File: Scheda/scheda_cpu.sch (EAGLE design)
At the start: 38 parts, among them IC2 LM3801N, IC3 LD1117V33

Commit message: modificato pcb
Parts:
- added H1, H2, H3: MOUNT-HOLE3.0, ITIS:MOUNT-HOLE3.0
- added LED: AK500, roombarmato_eagle_lib:AK500
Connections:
- net CHK_VBAT: now also IC1.A5; no longer IC1.A4
- net GND: now also LED.P$1
- net LED: now also IC1.A4, LED.P$2; no longer IC1.A5
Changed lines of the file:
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@@
 <part name="GND16" library="roombarmato_eagle_lib" deviceset="GND" device=""/>
 <part name="P+7" library="roombarmato_eagle_lib" deviceset="+12V" device=""/>
+<part name="LED" library="roombarmato_eagle_lib" deviceset="AK500" device="" package3d_urn="urn:adsk.eagle:package:17855270/2"/>
+<part name="GND17" library="roombarmato_eagle_lib" deviceset="GND" device=""/>
+<part name="H1" library="ITIS" deviceset="MOUNT-HOLE" device="3.0"/>
+<part name="H2" library="ITIS" deviceset="MOUNT-HOLE" device="3.0"/>
+<part name="H3" library="ITIS" deviceset="MOUNT-HOLE" device="3.0"/>
 </parts>
 <sheets>
@@
 <attribute name="VALUE" x="35.56" y="40.64" size="1.778" layer="96" rot="R90"/>
 </instance>
+<instance part="LED" gate="G$1" x="119.38" y="-34.29" smashed="yes">
+<attribute name="NAME" x="116.84" y="-27.94" size="1.27" layer="95"/>
+</instance>
+<instance part="GND17" gate="1" x="111.76" y="-40.64" smashed="yes">
+<attribute name="VALUE" x="109.22" y="-43.18" size="1.778" layer="96"/>
+</instance>
+<instance part="H1" gate="G$1" x="74.93" y="-30.48" smashed="yes">
+<attribute name="NAME" x="76.962" y="-29.8958" size="1.778" layer="95"/>
+<attribute name="VALUE" x="76.962" y="-32.9438" size="1.778" layer="96"/>
+</instance>
+<instance part="H2" gate="G$1" x="74.93" y="-36.83" smashed="yes">
+<attribute name="NAME" x="76.962" y="-36.2458" size="1.778" layer="95"/>
+<attribute name="VALUE" x="76.962" y="-39.2938" size="1.778" layer="96"/>
+</instance>
+<instance part="H3" gate="G$1" x="74.93" y="-43.18" smashed="yes">
+<attribute name="NAME" x="76.962" y="-42.5958" size="1.778" layer="95"/>
+<attribute name="VALUE" x="76.962" y="-45.6438" size="1.778" layer="96"/>
+</instance>
 </instances>
 <busses>
@@
 <pinref part="R10" gate="G$1" pin="P$1"/>
 <pinref part="GND16" gate="1" pin="GND"/>
+</segment>
+<segment>
+<pinref part="LED" gate="G$1" pin="P$1"/>
+<wire x1="113.03" y1="-36.83" x2="111.76" y2="-36.83" width="0.1524" layer="91"/>
+<pinref part="GND17" gate="1" pin="GND"/>
+<wire x1="111.76" y1="-38.1" x2="111.76" y2="-36.83" width="0.1524" layer="91"/>
 </segment>
 </net>
@@
 <net name="CHK_VBAT" class="0">
 <segment>
-<pinref part="IC1" gate="G$1" pin="A4"/>
-<wire x1="20.32" y1="-5.08" x2="21.59" y2="-5.08" width="0.1524" layer="91"/>
-<label x="21.59" y="-5.08" size="1.27" layer="95" xref="yes"/>
-</segment>
-<segment>
 <pinref part="R9" gate="G$1" pin="P$1"/>
 <pinref part="R10" gate="G$1" pin="P$2"/>
@@
 <label x="40.64" y="31.75" size="1.27" layer="95" xref="yes"/>
 </segment>
+<segment>
+<pinref part="IC1" gate="G$1" pin="A5"/>
+<wire x1="20.32" y1="-2.54" x2="21.59" y2="-2.54" width="0.1524" layer="91"/>
+<label x="21.59" y="-2.54" size="1.27" layer="95" xref="yes"/>
+</segment>
 </net>
 <net name="RD2" class="0">
@@
 <net name="LED" class="0">
 <segment>
-<pinref part="IC1" gate="G$1" pin="A5"/>
-<wire x1="20.32" y1="-2.54" x2="21.59" y2="-2.54" width="0.1524" layer="91"/>
-<label x="21.59" y="-2.54" size="1.27" layer="95" xref="yes"/>
-</segment>
-</net>
+<pinref part="LED" gate="G$1" pin="P$2"/>
+<wire x1="113.03" y1="-31.75" x2="111.76" y2="-31.75" width="0.1524" layer="91"/>
+<label x="111.76" y="-31.75" size="1.27" layer="95" rot="R180" xref="yes"/>
+</segment>
+<segment>
+<pinref part="IC1" gate="G$1" pin="A4"/>
+<wire x1="20.32" y1="-5.08" x2="21.59" y2="-5.08" width="0.1524" layer="91"/>
+<label x="21.59" y="-5.08" size="1.27" layer="95" xref="yes"/>
+</segment>
+</net>

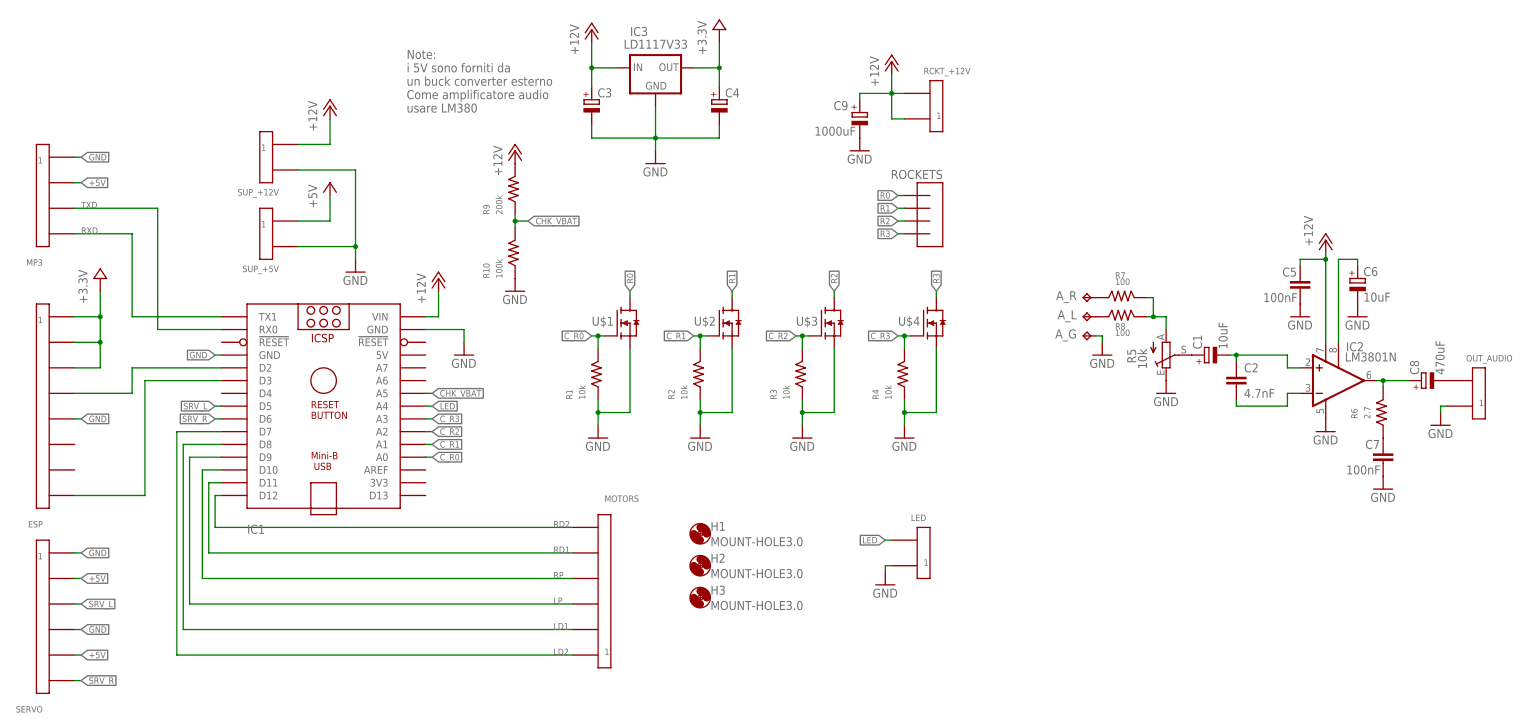
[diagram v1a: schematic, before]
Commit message: modificato leggermente pcb, cambiato package lm380
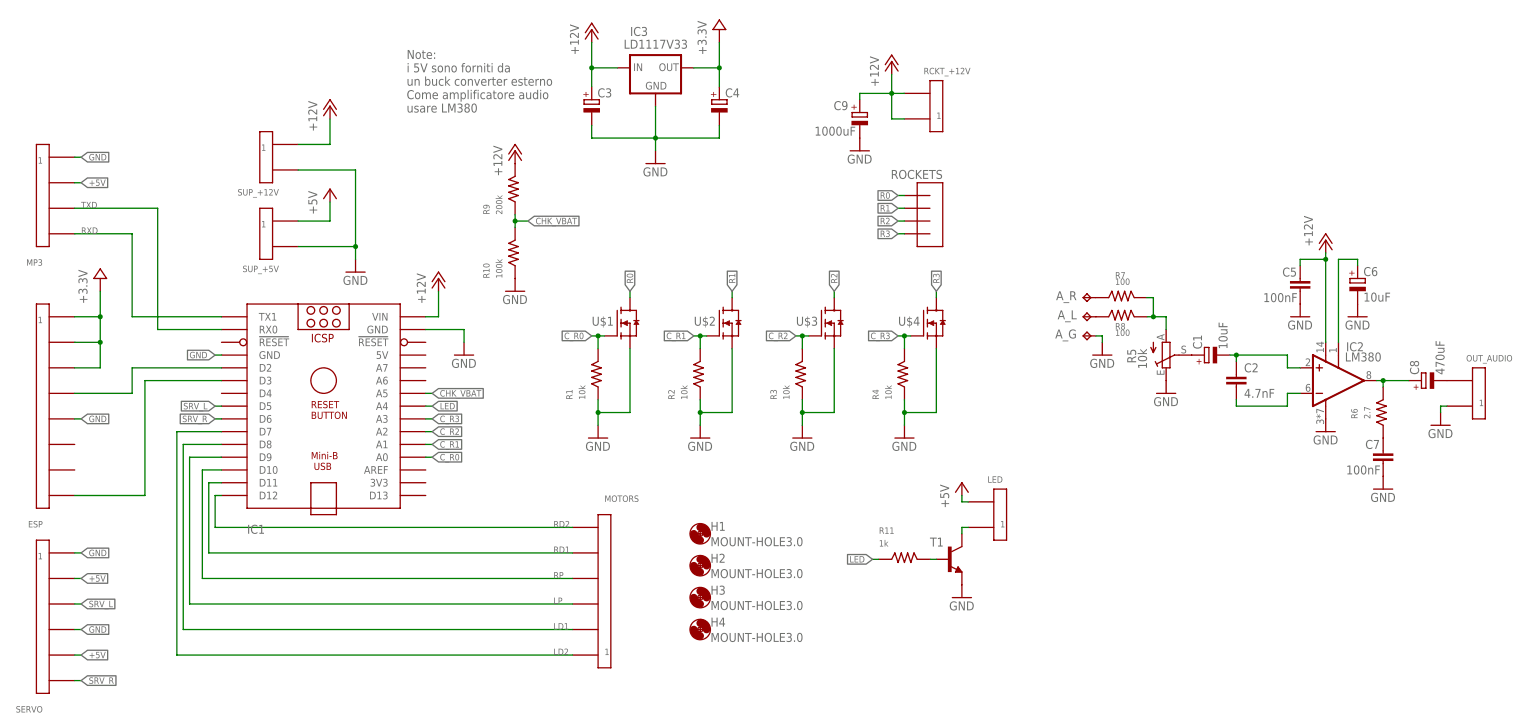
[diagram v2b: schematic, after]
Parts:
- added H4: MOUNT-HOLE3.0, ITIS:MOUNT-HOLE3.0
- added R11: 1k, roombarmato_eagle_lib:RESISTOR1206
- added T1: BC-817, CiniTechLibrary:BC-817
- IC2: value LM3801N -> LM380; device roombarmato_eagle_lib:LM3801N -> roombarmato_eagle_lib:LM380
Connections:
- new net N$2: LED.P$1, T1.C
- new net N$3: R11.P$2, T1.B
- net +5V: now also LED.P$2
- net GND: now also T1.E; no longer LED.P$1
- net LED: now also R11.P$1; no longer LED.P$2
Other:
- moved on the sheet: IC2, LED

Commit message: sistemato pcb
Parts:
- removed C4: (no value), roombarmato_eagle_lib:CPOL-EUE2.5-5
- removed OUT_AUDIO, RCKT_+12V, SUP_+12V, SUP_+5V: AK500, roombarmato_eagle_lib:AK500
- added C10: 100nF, ITIS:C-EU025-030X050
- added C11: 10uF, ITIS:CPOL-EUE2-4
- added OUT-AUDIO, RCKT-12, SUP-12, SUP-5, SWITCH: MORSETTIERE-2, CyberLibrary:MORSETTIERE-2
- C3: value (none) -> 22uF; device roombarmato_eagle_lib:CPOL-EUE2.5-5 -> ITIS:CPOL-EUE2-4
- IC3: value LD1117V33 -> AMS1117-3.3V; device roombarmato_eagle_lib:78XXS -> roombarmato_eagle_lib:AMS1117
- LED: value AK500 -> MORSETTIERE-2; device roombarmato_eagle_lib:AK500 -> CyberLibrary:MORSETTIERE-2
- renumbered U$1 to T2, U$2 to T3, U$3 to T4, U$4 to T5
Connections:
- removed net N$17: C8.-, OUT_AUDIO.P$2
- new net N$11: C8.-, OUT-AUDIO.B
- new net SWITCH: IC1.A4, SWITCH.B
- net +12V: now also RCKT-12.A, RCKT-12.B, SUP-12.A; no longer C3.+, IC3.IN, RCKT_+12V.P$1, RCKT_+12V.P$2, SUP_+12V.P$1
- net +3.3V: now also C10.1, C3.+; no longer C4.+
- net +5V: now also C11.+, IC3.IN, LED.A, SUP-5.A; no longer LED.P$2, SUP_+5V.P$1
- net CHK_VBAT: now also IC1.A6; no longer IC1.A5
- net GND: now also C10.2, C11.-, OUT-AUDIO.A, SUP-12.B, SUP-5.B, SWITCH.A; no longer C4.-, OUT_AUDIO.P$1, SUP_+12V.P$2, SUP_+5V.P$2
- net LED: now also IC1.A5; no longer IC1.A4
- net N$2: now also LED.B; no longer LED.P$1
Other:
- moved on the sheet: C3, C9, LED

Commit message: sistemato pcb e ordine
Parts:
- C10, C2, C5, C7: device ITIS:C-EU025-030X050 -> ITIS:C-EUC1206
- R5: value 10k -> 100k
- R7, R8: value 100 -> 1k

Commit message: completato PCB
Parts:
- R5: value 100k -> 50k; device pot:TRIM_EU-S64W -> rcl:R-TRIMM3314J
